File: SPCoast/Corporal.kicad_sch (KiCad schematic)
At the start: 36 parts, among them SW11829 829, SW11831 831, SW11900 829D, SW11901 1

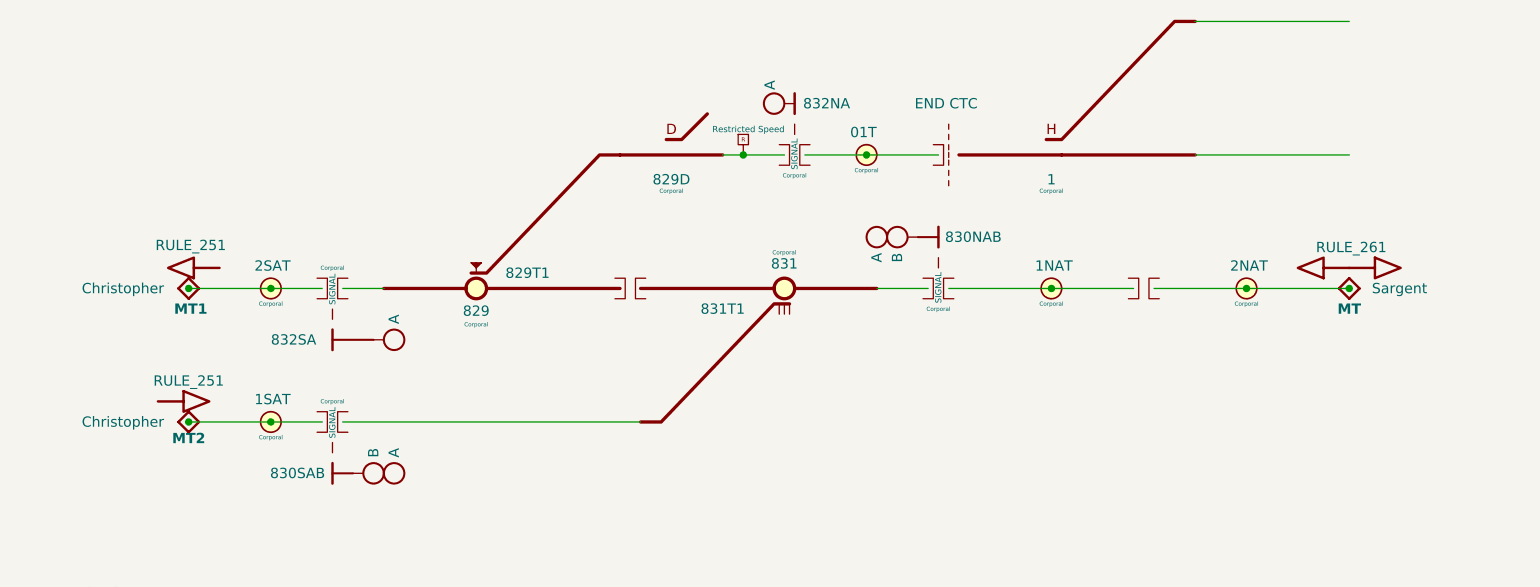
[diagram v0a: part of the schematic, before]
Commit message: chore(kicad): SPCoast symbols refreshed, field attribute visibility, no-connects on unused pins (owner's edit, baseline)
Owner, 2026-10-08: updated symbols from the libraries (the field pin direction flip, InterlockingPlant
61269e0), adjusted attribute visibility, added 22 no-connect markers on unused pins.

Verified (committed as saved, no edits):
- 485 components, 648 nets; every net identical to the previous commit.
- ERC 53 -> 20 messages (13 errors, 7 warnings). Remaining: unconnected HOUSE H / aux MC pins
  (Gilroy Caltrain, Luchessa, Watsonville); Corporal SW11901 still Railroad:Switch_HandThrow (not in
  the library) with open N/R legs; Sargent switch 1 open N/R legs; Christopher Panel U10029 A6 open
  while lamp LMP10093 carries a no-connect; 5 inherited wire stubs.
- Every instance path starts at the root uuid.

Co-Authored-By: Claude Opus 5.5 <noreply@anthropic.com>
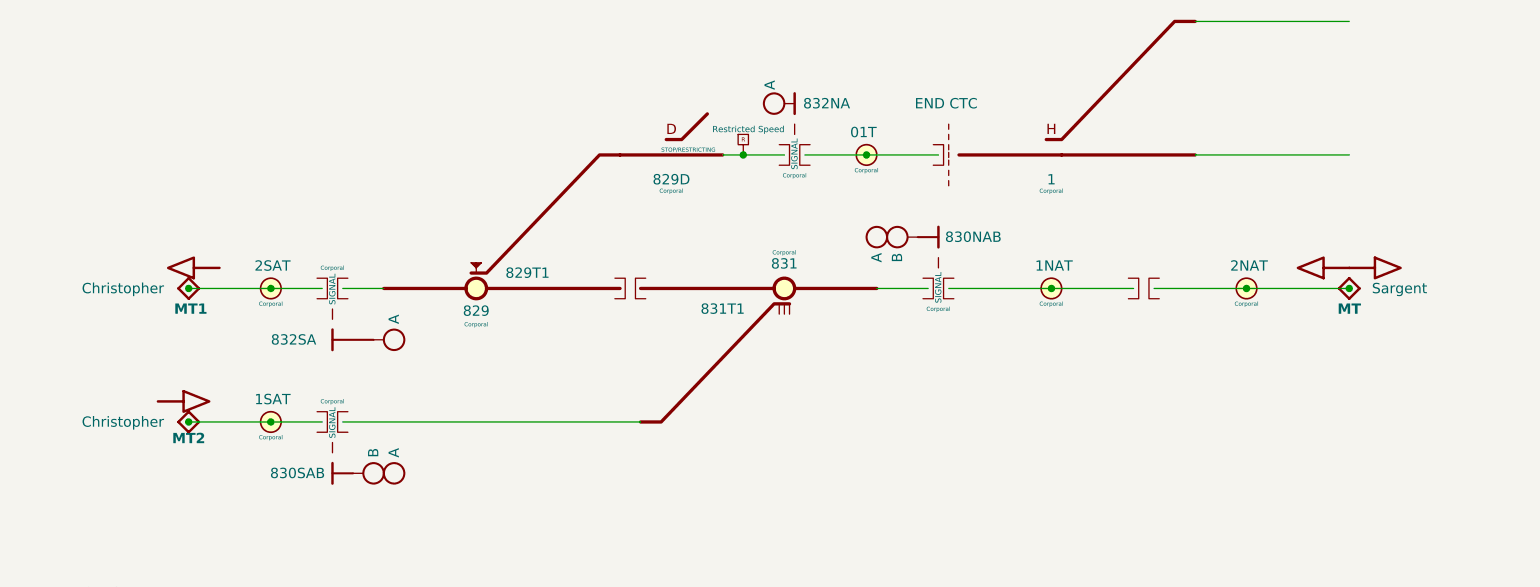
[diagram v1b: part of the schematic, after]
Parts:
- SW11900: Indications (none) -> STOP/RESTRICTING
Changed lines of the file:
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@@
 		)
 		(property "CP" "Corporal"
-			(at 123.19 73.03 0)
+			(at 123.19 73.025 0)
 			(show_name no)
 			(do_not_autoplace no)
@@
 			)
 		)
+		(property "Indications" "STOP/RESTRICTING"
+			(at 121.92 67.945 0)
+			(show_name no)
+			(do_not_autoplace no)
+			(effects
+				(font
+					(size 0.508 0.508)
+				)
+				(justify left)
+			)
+		)
 		(pin "2"
 		)
@@
 		)
 		(property "CP" "Corporal"
-			(at 99.06 89.54 0)
+			(at 99.06 89.535 0)
 			(show_name no)
 			(do_not_autoplace no)
@@
 		)
 		(property "TC" "${VALUE}T1"
-			(at 105.41 83.19 0)
+			(at 105.41 83.185 0)
 			(show_name no)
 			(do_not_autoplace no)
@@
 		)
 		(property "Role" "APPLIANCE"
-			(at 99.06 85.09 0)
+			(at 92.075 78.74 0)
 			(hide yes)
 			(show_name no)
@@
 		)
 		(property "Kind" "SWITCH_LOCK"
-			(at 99.06 85.09 0)
+			(at 93.345 80.645 0)
 			(hide yes)
 			(show_name no)
@@
 			)
 		)
+		(property "Indications" ""
+			(at 112.395 84.455 0)
+			(show_name no)
+			(do_not_autoplace no)
+			(effects
+				(font
+					(size 0.508 0.508)
+				)
+			)
+		)
 		(pin "3"
 		)
@@
 		)
 		(property "Kind" "RULE_251"
-			(at 63.754 79.756 0)
+			(at 63.5 82.55 0)
+			(hide yes)
 			(show_name no)
 			(do_not_autoplace no)
@@
 		)
 		(property "CP" "Corporal"
-			(at 194.31 86.99 0)
+			(at 194.31 86.995 0)
 			(show_name no)
 			(do_not_autoplace no)
@@
 		)
 		(property "CP" "Corporal"
-			(at 147.32 70.48 0)
+			(at 147.32 70.485 0)
 			(show_name no)
 			(do_not_autoplace no)
@@
 		)
 		(property "CP" "Corporal"
-			(at 73.66 86.99 0)
+			(at 73.66 86.995 0)
 			(show_name no)
 			(do_not_autoplace no)
@@
 		)
 		(property "Kind" "RULE_251"
-			(at 63.5 96.52 0)
+			(at 63.5 99.06 0)
+			(hide yes)
 			(show_name no)
 			(do_not_autoplace no)
@@
 		)
 		(property "CP" "Corporal"
-			(at 137.16 80.64 0)
+			(at 137.16 80.645 0)
 			(show_name no)
 			(do_not_autoplace no)
@@
 			(at 129.54 87.63 0)
 			(show_name no)
-			(do_not_autoplace no)
+			(do_not_autoplace yes)
 			(effects
 				(font
@@
 		)
 		(property "Role" "APPLIANCE"
-			(at 137.16 85.09 0)
+			(at 145.415 92.71 0)
 			(hide yes)
 			(show_name no)
@@
 		)
 		(property "Kind" "SWITCH_REMOTE"
-			(at 137.16 85.09 0)
+			(at 142.875 90.805 0)
 			(hide yes)
 			(show_name no)
@@
 			)
 		)
+		(property "Indications" ""
+			(at 123.825 85.725 0)
+			(show_name no)
+			(do_not_autoplace no)
+			(effects
+				(font
+					(size 0.508 0.508)
+				)
+			)
+		)
 		(pin "2"
 		)
@@
 		)
 		(property "CP" "Corporal"
-			(at 170.18 86.99 0)
+			(at 170.18 86.995 0)
 			(show_name no)
 			(do_not_autoplace no)
@@
 		)
 		(property "CP" "Corporal"
-			(at 73.66 103.5 0)
+			(at 73.66 103.505 0)
 			(show_name no)
 			(do_not_autoplace no)
@@
 		)
 		(property "Kind" "RULE_261"
-			(at 207.264 80.01 0)
+			(at 207.01 82.55 0)
+			(hide yes)
 			(show_name no)
 			(do_not_autoplace no)

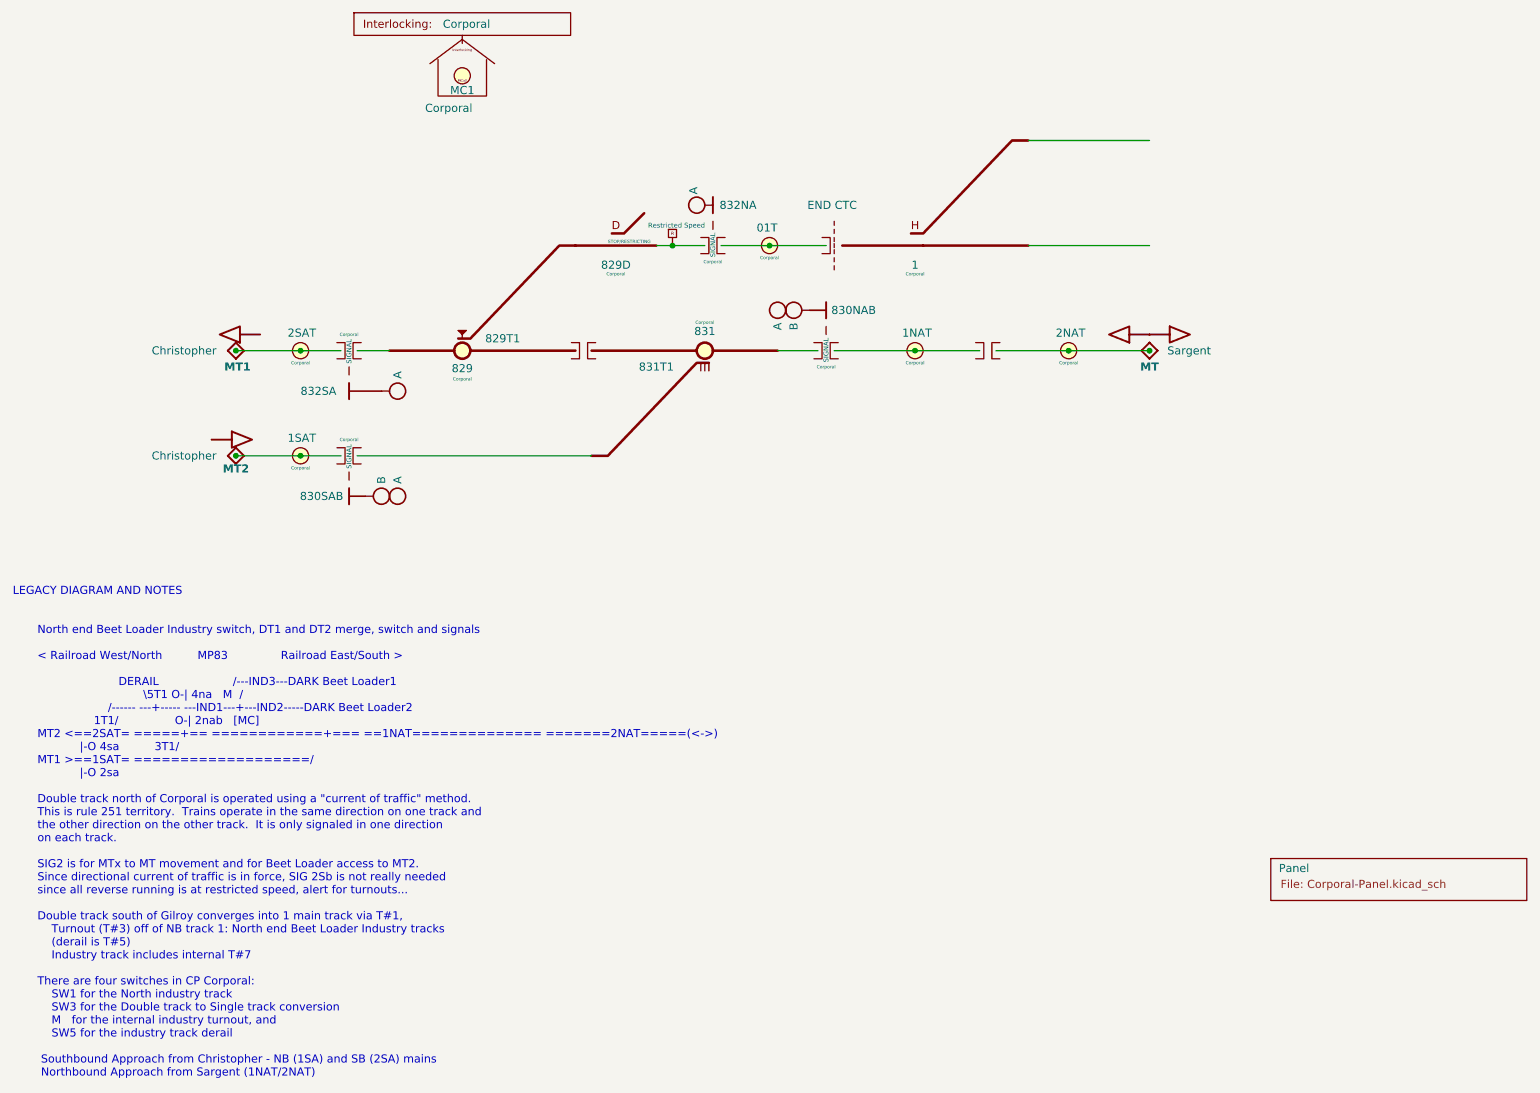
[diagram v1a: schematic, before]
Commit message: fix(kicad): SPCoast ERC clean: Corporal SW11901 to Switch_Manual_Sensed, Christopher lamp fixed, no-connects (owner's edit, baseline)
Owner, 2026-10-08. Corporal and Sargent's industry tracks (the beet loader) join each other outside
CTC: dark track, no routes, no NextCP.

Verified (committed as saved, no edits): 485 components, 648 nets; ERC 0 errors, 0 warnings.

Co-Authored-By: Claude Opus 5.5 <noreply@anthropic.com>
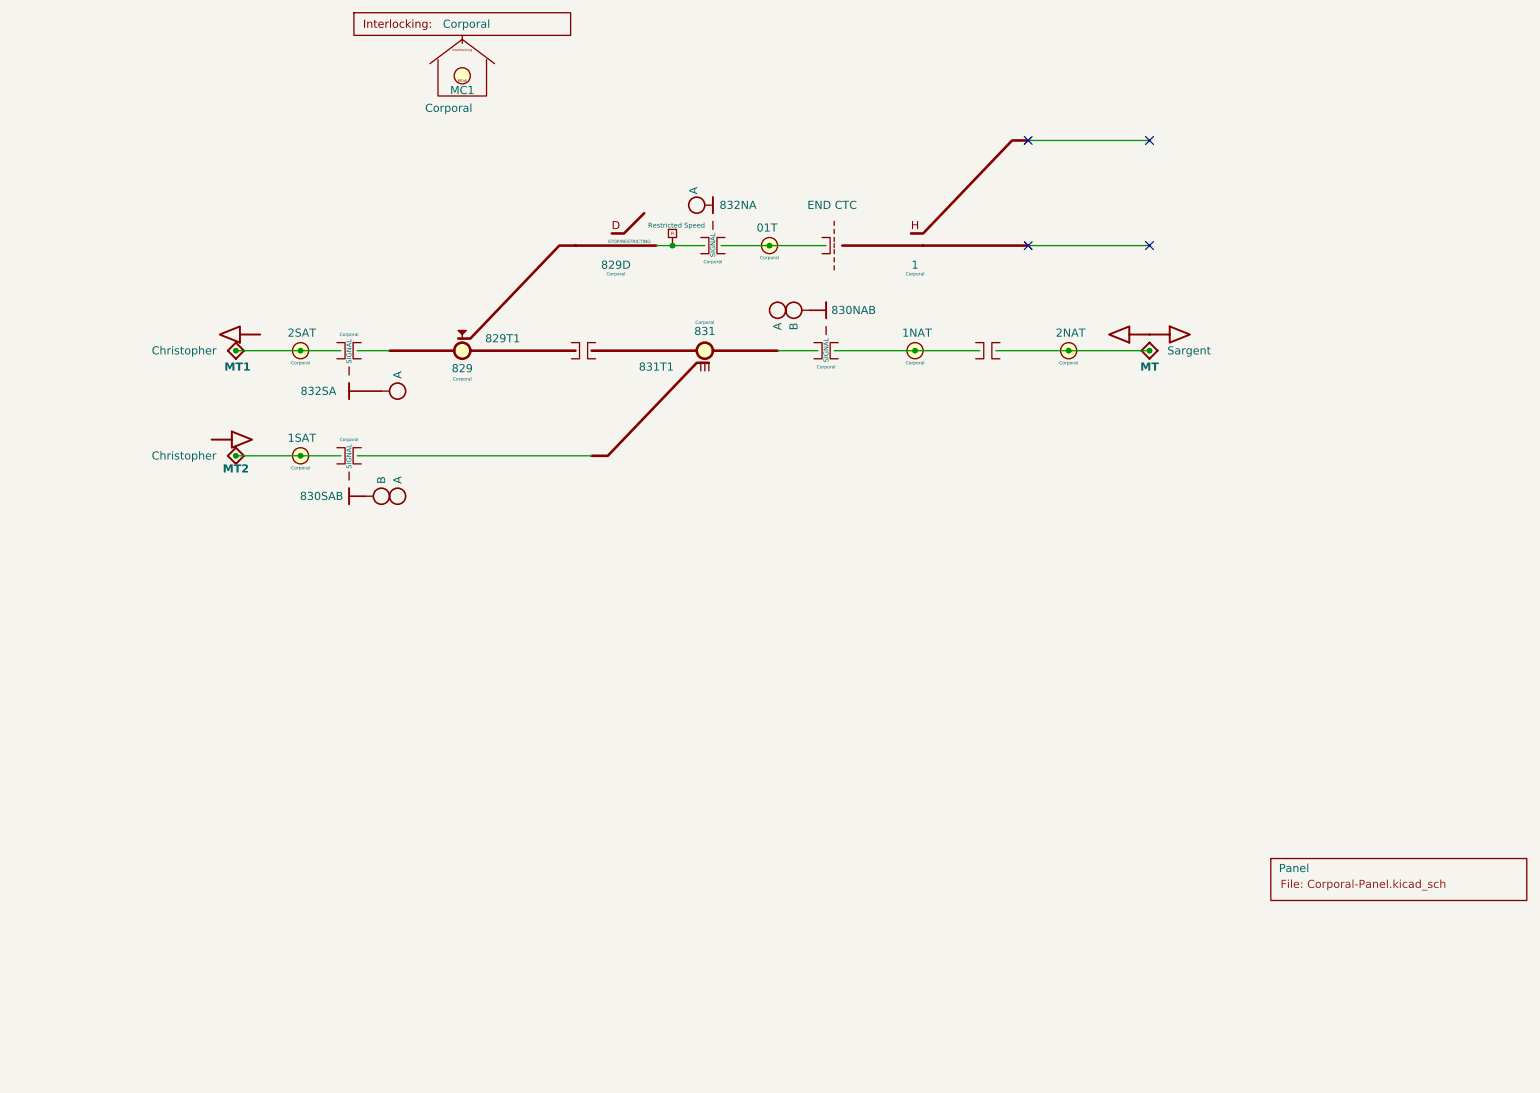
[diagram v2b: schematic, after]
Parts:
- SW11901: symbol Railroad:Switch_HandThrow -> Railroad:Switch_Manual_Sensed
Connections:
- no-connect marks 0 -> 4
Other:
- note removed: "LEGACY DIAGRAM AND NOTES North end Beet Loader Industry switch, DT1 and DT2 merge, switch and signals < Railroad West/North MP83 Railroad East/South > DERAIL /---IND3---DARK Beet Loader1 \5T1 O-| 4na M / /------ ---+----- ---IND1---+---IND2-----DARK Beet Loader2 1T1/ O-| 2nab [MC] MT2 <==2SAT= =====+== ============+=== ==1NAT============== =======2NAT=====(<->) |-O 4sa 3T1/ MT1 >==1SAT= =========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"
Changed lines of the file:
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@@
 		(comment 9 "active")
-	)
-	(text "LEGACY DIAGRAM AND NOTES\n\n   \n       North end Beet Loader Industry switch, DT1 and DT2 merge, switch and signals\n   \n       < Railroad West/North          MP83               Railroad East/South >\n   \n                              DERAIL                     /---IND3---DARK Beet Loader1\n                                     \\5T1 O-| 4na   M  /\n                           /------ ---+----- ---IND1---+---IND2-----DARK Beet Loader2\n                       1T1/                O-| 2nab   [MC]\n       MT2 <==2SAT= =====+== ============+=== ==1NAT============== =======2NAT=====(<->)\n                   |-O 4sa          3T1/\n       MT1 >==1SAT= ===================/\n                   |-O 2sa\n   \n       Double track north of Corporal is operated using a \"current of traffic\" method.\n       This is rule 251 territory.  Trains operate in the same direction on one track and\n       the other direction on the other track.  It is only signaled in one direction\n       on each track.\n   \n       SIG2 is for MTx to MT movement and for Beet Loader access to MT2.\n       Since directional current of traffic is in force, SIG 2Sb is not really needed\n       since all reverse running is at restricted speed, alert for turnouts...\n   \n       Double track south of Gilroy converges into 1 main track via T#1,\n           Turnout (T#3) off of NB track 1: North end Beet Loader Industry tracks\n           (derail is T#5)\n           Industry track includes internal T#7\n   \n       There are four switches in CP Corporal:\n           SW1 for the North industry track\n           SW3 for the Double track to Single track conversion\n           M   for the internal industry turnout, and\n           SW5 for the industry track derail\n   \n        Southbound Approach from Christopher - NB (1SA) and SB (2SA) mains\n        Northbound Approach from Sargent (1NAT/2NAT)"
-		(exclude_from_sim no)
-		(at 28.448 160.782 0)
-		(effects
-			(font
-				(size 1.27 1.27)
-			)
-			(justify left)
-		)
 	)
 	(junction
@@
 		(diameter 0)
 		(color 0 0 0 0)
+	)
+	(no_connect
+		(at 207.01 68.58)
+	)
+	(no_connect
+		(at 207.01 52.07)
+	)
+	(no_connect
+		(at 187.96 52.07)
+	)
+	(no_connect
+		(at 187.96 68.58)
 	)
 	(wire
@@
 	)
 	(symbol
-		(lib_id "Railroad:Switch_HandThrow")
+		(lib_id "Railroad:Switch_Manual_Sensed")
 		(at 170.18 68.58 0)
 		(unit 1)
@@
 		)
 		(property "Description" ""
-			(at 170.18 68.58 0)
+			(at 171.45 77.47 0)
 			(hide yes)
 			(show_name no)
@@
 		)
 		(property "CP" "Corporal"
-			(at 170.18 73.03 0)
+			(at 170.18 73.025 0)
 			(show_name no)
 			(do_not_autoplace no)
@@
 			(at 177.8 66.04 0)
 			(show_name no)
-			(do_not_autoplace no)
+			(do_not_autoplace yes)
 			(effects
 				(font
@@
 		)
 		(property "Role" "APPLIANCE"
-			(at 170.18 68.58 0)
+			(at 168.275 73.025 0)
 			(hide yes)
 			(show_name no)
@@
 		)
 		(property "Kind" "SWITCH_MANUAL"
-			(at 170.18 68.58 0)
-			(hide yes)
-			(show_name no)
-			(do_not_autoplace no)
-			(effects
-				(font
-					(size 1.27 1.27)
-				)
-			)
+			(at 168.91 74.93 0)
+			(hide yes)
+			(show_name no)
+			(do_not_autoplace no)
+			(effects
+				(font
+					(size 1.27 1.27)
+				)
+			)
+		)
+		(property "Indications" ""
+			(at 181.61 67.945 0)
+			(show_name no)
+			(do_not_autoplace yes)
+			(effects
+				(font
+					(size 0.508 0.508)
+				)
+			)
